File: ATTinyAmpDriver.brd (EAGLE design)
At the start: 30 x 15 mm, 25 parts, among them Q1 SI2301CDS, T1 BC846, U1 SPX5205M5-L-3-3, U2 ATTINY5-TSHR, U3 MCP6001, X1 DIODES, X2 INPUT

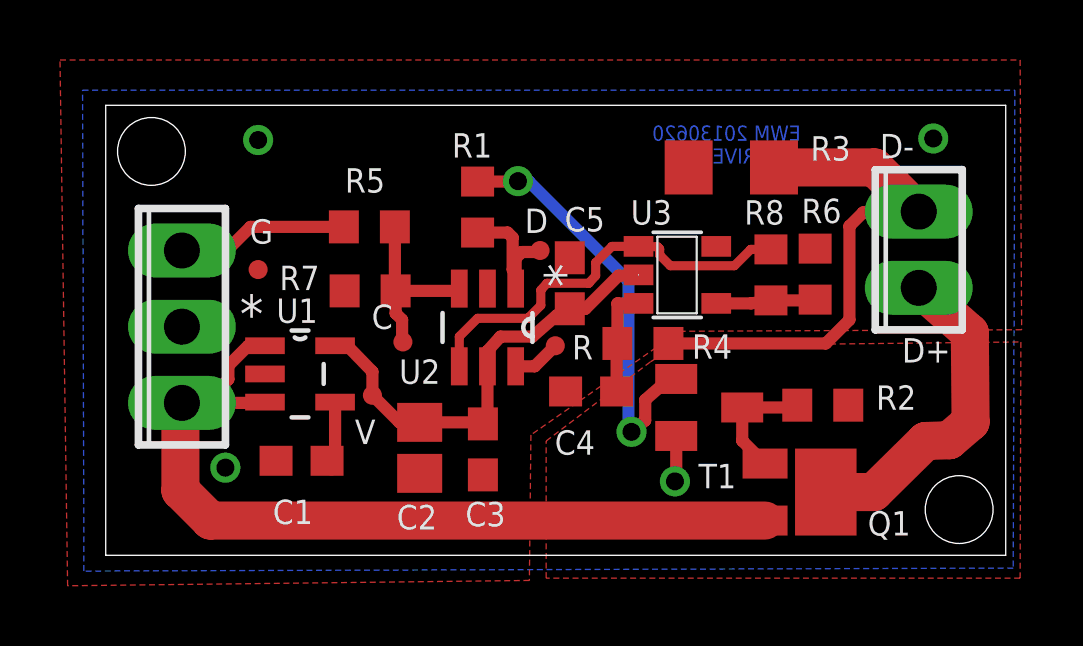
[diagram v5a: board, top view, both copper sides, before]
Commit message: Changed PWM filter to Sallen Key
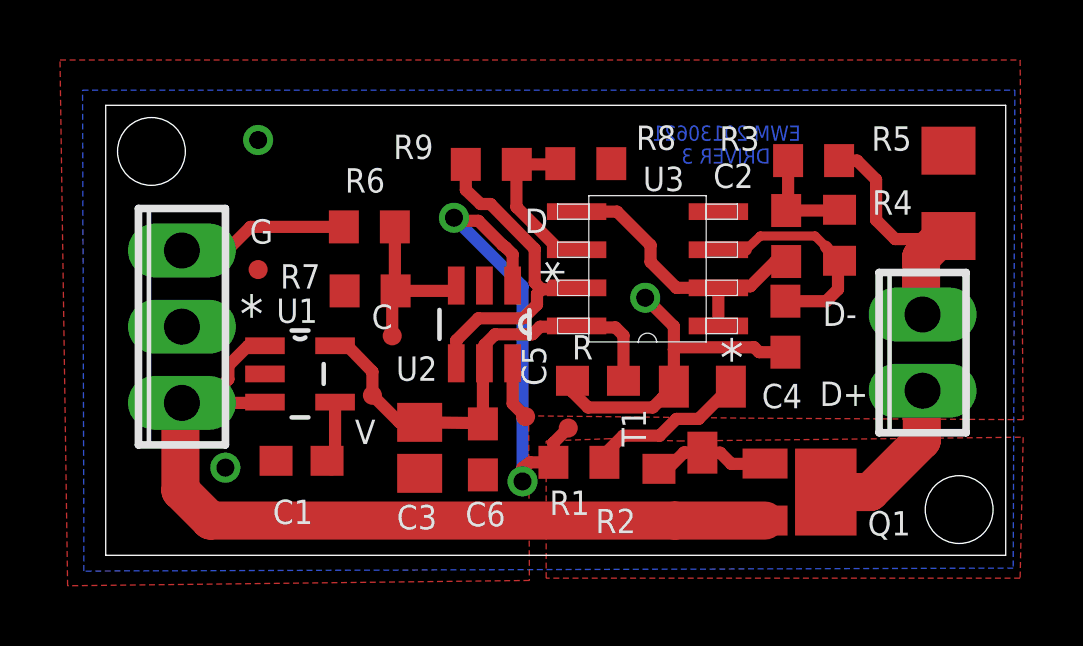
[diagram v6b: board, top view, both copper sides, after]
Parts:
- added C6: .1u, resistor:C0603
- added R9: 28.7K, resistor:R0603
- C2: value 10u -> .1u; device resistor:C0805 -> resistor:C0603
- C3: value .1u -> 10u; device resistor:C0603 -> resistor:C0805
- R3: value .1 -> 10k; device resistor:R1206 -> resistor:R0603
- R5: value 3.2k -> .1; device resistor:R0603 -> resistor:R1206
- R6: value 1K -> 3.2k
- R8: value 28.7K -> 1K
- U3: value MCP6001 -> MCP6L2-X_SN; device Combined:SOT23-5 -> Combined:SOIC8-N_MC
- moved R5 19.3 mm to (28.1, 12.1), turned to 270 degrees
- moved R6 14.9 mm to (8.79, 10.9), turned to 180 degrees
- moved C2 14.1 mm to (22.7, 10.6), turned to 90 degrees
- moved R1 9.16 mm to (15.8, 3.10), turned to 0 degrees
- moved R4 7.48 mm to (24.5, 10.7), turned to 270 degrees
- moved R8 7.20 mm to (16.0, 13.1), turned to 180 degrees
- moved C4 6.83 mm to (22.7, 7.62), turned to 270 degrees
- moved R2 6.22 mm to (18.4, 2.03), turned to 90 degrees
- moved TPIDATA 5.99 mm to (15.4, 4.24)
- moved X1 3.43 mm to (27.2, 6.76)
- moved C5 3.38 mm to (16.4, 5.82), turned to 180 degrees
- moved R3 2.75 mm to (23.6, 13.2), turned to 180 degrees
- moved RESET 2.56 mm to (14.0, 4.62)
- moved C3 2.11 mm to (10.5, 3.58)
- moved U3 1.01 mm to (18.1, 9.55), turned to 180 degrees
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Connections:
- net N$7 renamed INA+
- removed net N$4: R6.2, R8.2, U3.4
- new net N$8: C2.2, R3.2, R4.1
- new net OUTA: C2.1, U3.1, U3.2, U3.5
- new net VINB-: R8.2, R9.2, U3.6
- net BLINK: now also R6.1; no longer R5.1
- net D-: now also R3.1, R5.2; no longer R3.2, R4.1
- net GND: now also C6.2, R5.1, R8.1, U3.4; no longer C2.2, R3.1, R6.1, U3.5
- net MEASURE: now also R9.1, U3.7; no longer R8.1, U3.1
- net N$1: now also R6.2; no longer R5.2
- net VCC: now also C6.1, U3.8; no longer C2.1, U3.2
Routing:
- net MOSFET: track 4.38 -> 16.1 mm, vias 0 -> 2
- net OUTA: track 0.00 -> 10.00 mm
- net GND: track 1.54 -> 11.4 mm, vias 4 -> 3
- net D-: track 17.4 -> 8.70 mm
- net N$6: track 14.1 -> 5.42 mm, vias 2 -> 0
- net VINB-: track 0.00 -> 5.48 mm
- net N$3: track 11.0 -> 5.58 mm
- net INA+: track 3.67 -> 7.46 mm
- net N$8: track 0.00 -> 3.48 mm
- net N$4: track 3.32 -> 0.00 mm
- net MEASURE: track 13.8 -> 11.1 mm
- net VCC: track 15.3 -> 15.8 mm
- net +14V: track 28.7 -> 29.2 mm
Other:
- board text added: "EWM 20130621 AT DRIVER 3"
- board text removed: "EWM 20130620 AT DRIVER 3"

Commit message: Added a diode to Blink input to prevent back feed if transistor shorts
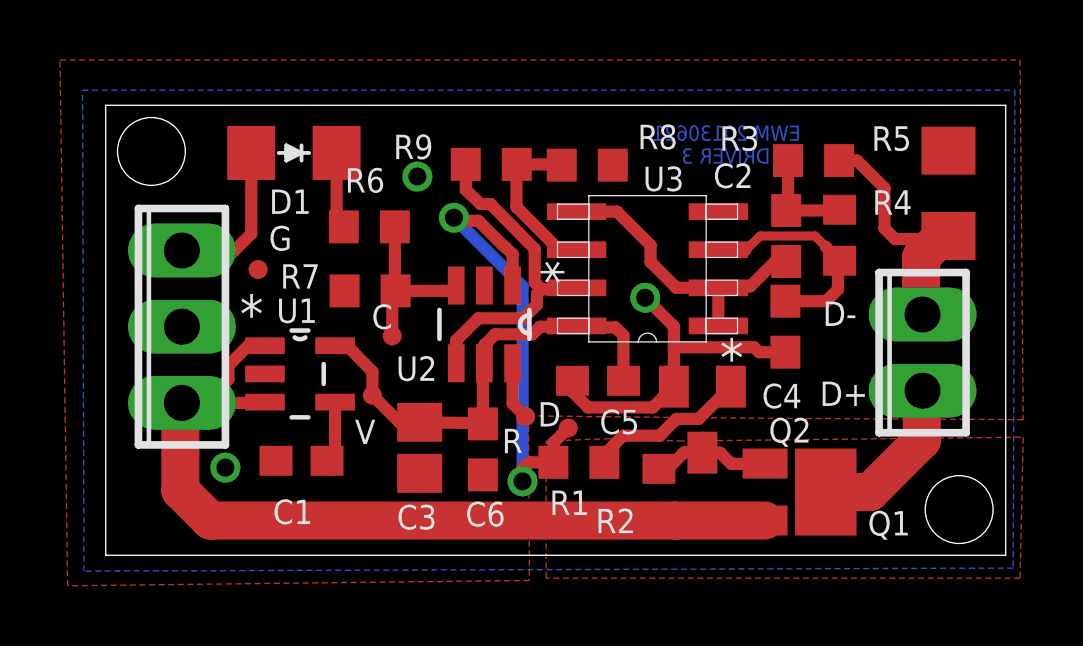
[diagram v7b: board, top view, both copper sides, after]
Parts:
- added D1: CD1206-B260, Combined:D1206
- R6: value 3.2k -> 3.3k
- R8: value 1K -> 1k
- moved R8 0.07 mm to (16.1, 13.0), turned to 0 degrees
- renumbered T1 to Q2
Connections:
- new net N$4: D1.1, R6.2
- net GND: now also R8.2; no longer R8.1
- net N$1: now also D1.2; no longer R6.2
- net VINB-: now also R8.1; no longer R8.2
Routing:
- net N$4: track 0.00 -> 2.56 mm

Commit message: Changed blink diode to regular rectifier diode
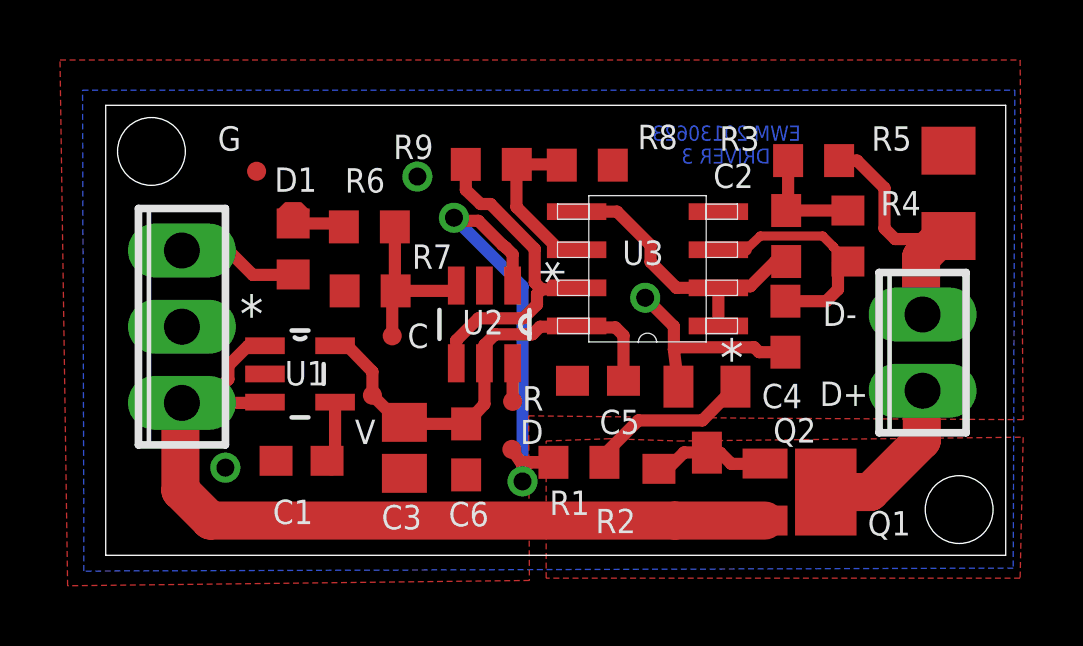
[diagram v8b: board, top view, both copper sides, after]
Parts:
- D1: value CD1206-B260 -> DIODE_0603; device Combined:D1206 -> Combined:D0603
- moved GND 3.28 mm to (5.03, 12.8)
- moved D1 3.20 mm to (6.25, 10.2), turned to 90 degrees
- moved TPIDATA 2.01 mm to (13.5, 3.53)
- moved RESET 0.67 mm to (13.6, 5.13)
- moved C6 0.56 mm to (12.0, 3.53)
- moved C3 0.51 mm to (9.96, 3.58)
- moved R4 0.28 mm to (24.7, 10.6)
- moved Q2 0.15 mm to (20.0, 4.52)
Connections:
- net N$1: now also D1.1A; no longer D1.2
- net N$4: now also D1.2C; no longer D1.1
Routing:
- net GND: track 11.4 -> 7.19 mm
- net N$1: track 5.28 -> 4.05 mm
- net N$4: track 2.56 -> 1.74 mm
- net RESET: track 1.96 -> 1.27 mm
- net INA+: track 7.46 -> 8.03 mm
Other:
- board text added: "EWM 20130623 AT DRIVER 3"
- board text removed: "EWM 20130621 AT DRIVER 3"
